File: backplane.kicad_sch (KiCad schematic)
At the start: 2 parts, among them J200 09031967921, U200 PESD5V0S2BT

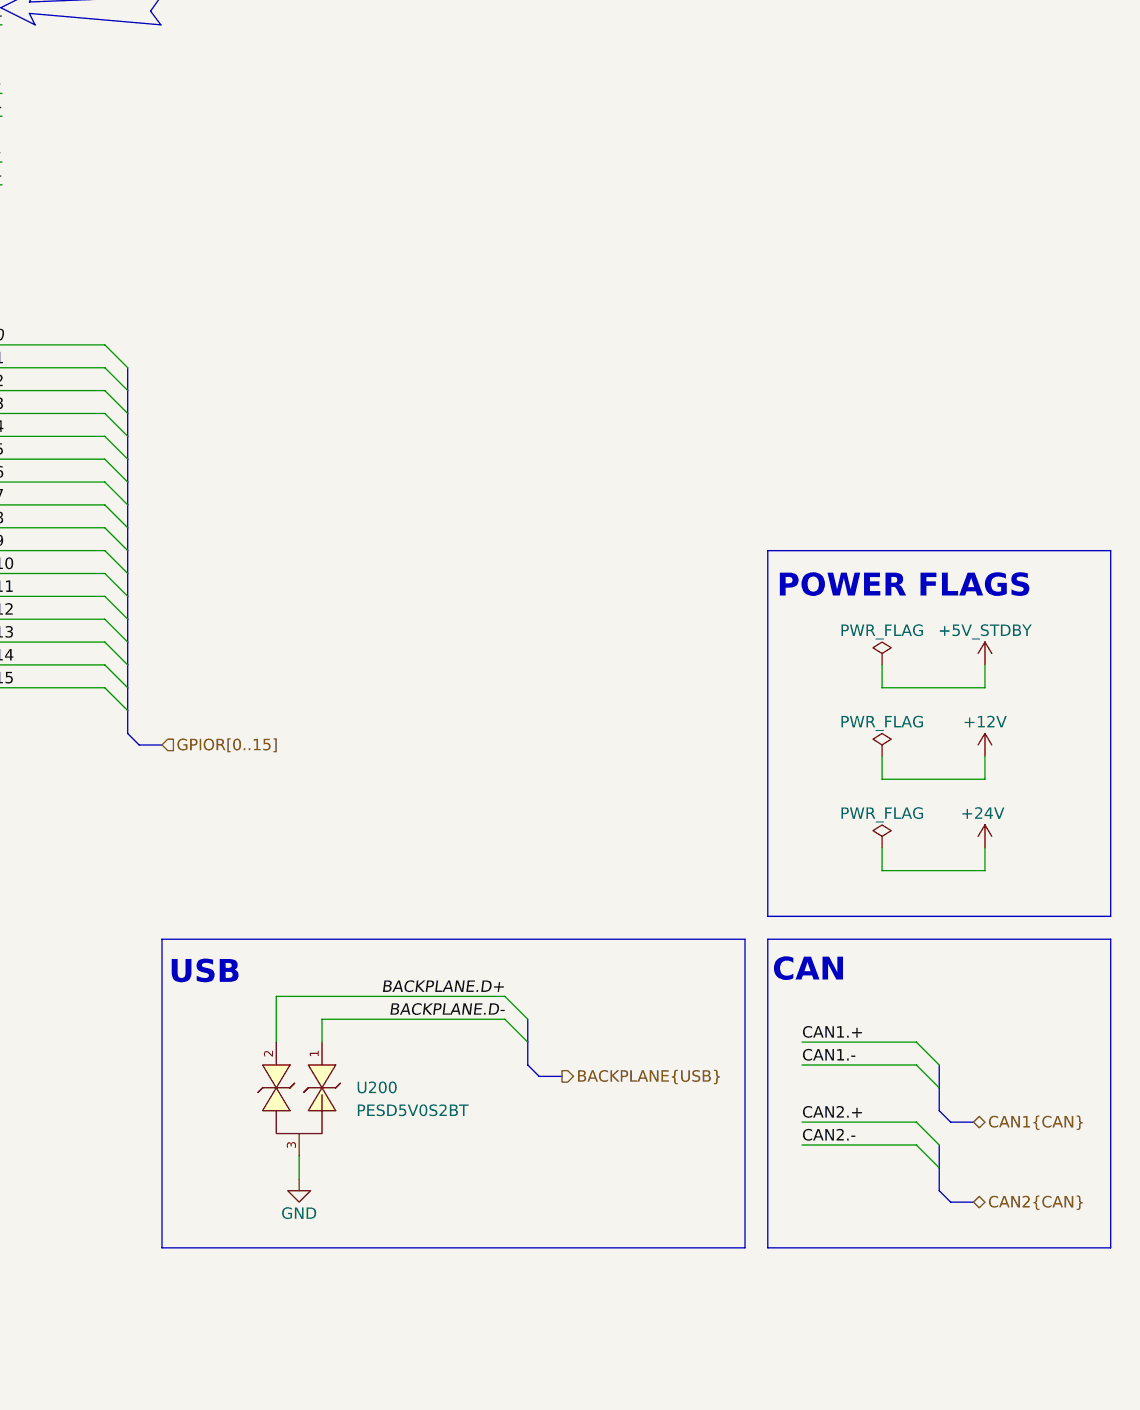
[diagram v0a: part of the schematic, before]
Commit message: change LED Indicator
also most wide tracks changed to polygons
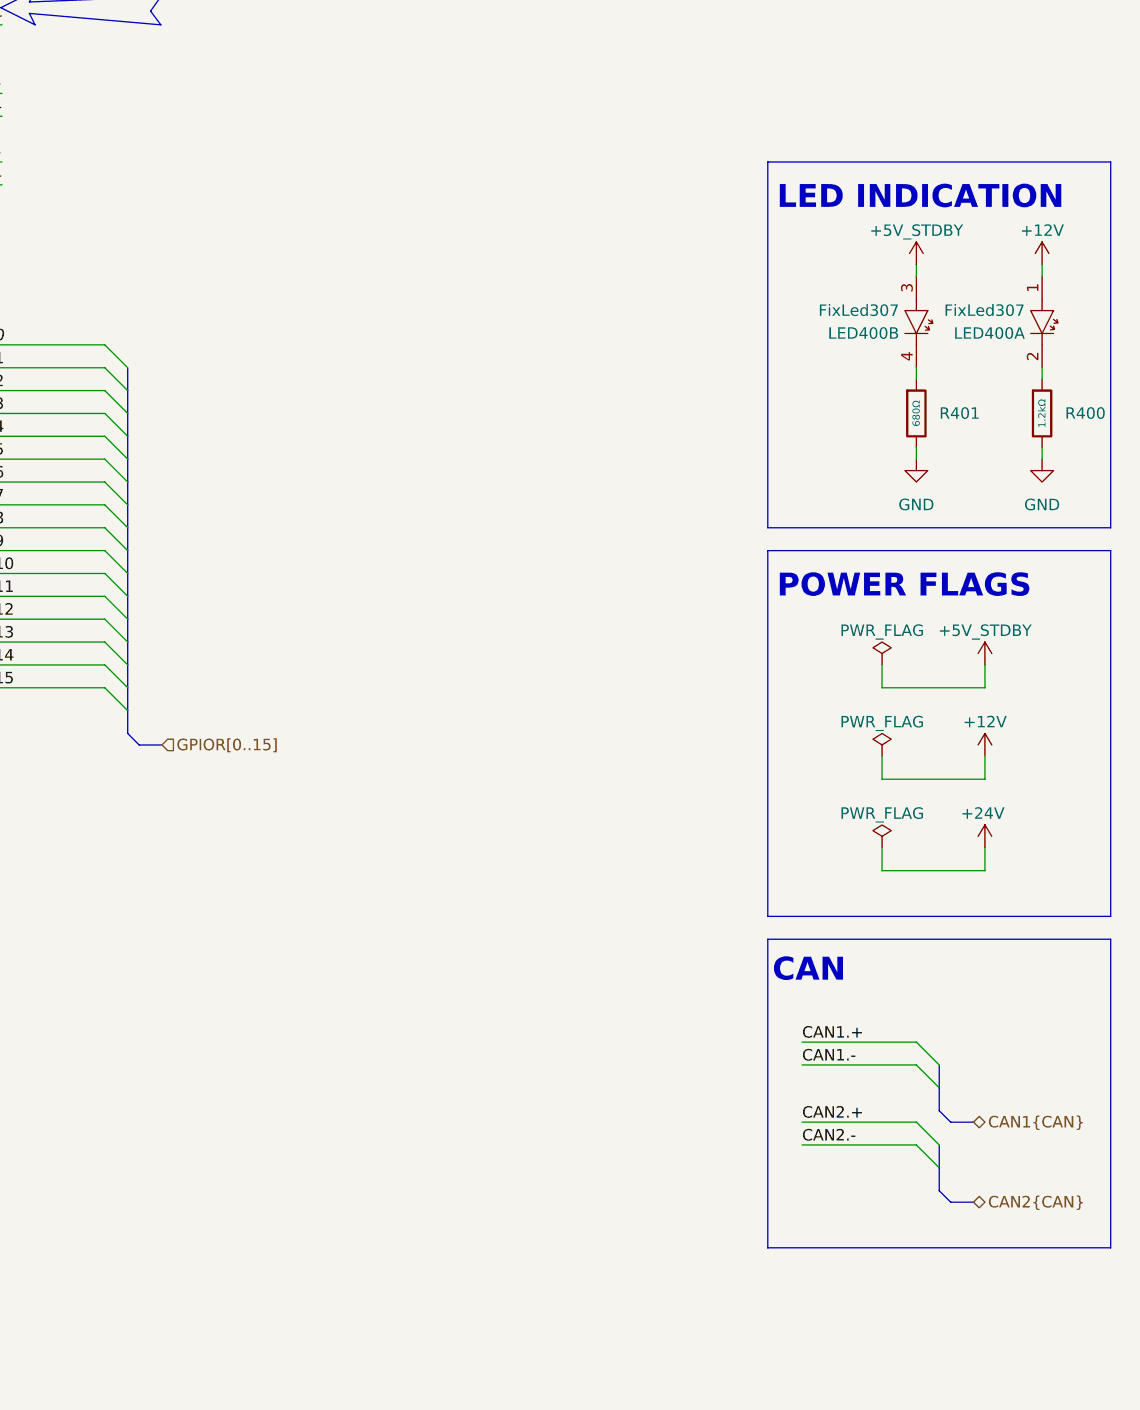
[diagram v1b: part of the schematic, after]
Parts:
- removed U200: PESD5V0S2BT, Package_TO_SOT_SMD:SOT-23, symbol PESD5V0S2BT:PESD5V0S2BT
- added LED400: FixLed307, FixLed307:FixLed307, symbol FixLed307:FixLed307
- added R400: 1.2kΩ, PCM_JLCPCB:R_0805, symbol PCM_JLCPCB-Resistors:0805,1.2kΩ
- added R401: 680Ω, PCM_JLCPCB:R_0805, symbol PCM_JLCPCB-Resistors:0805,680Ω
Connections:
- net +12V: now also LED400.1
- net +5V_STDBY: now also LED400.3
- net GND: now also R400.2, R401.2
- new net: LED400.2, R400.1
- new net: LED400.4, R401.1
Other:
- note added: "LED INDICATION"
